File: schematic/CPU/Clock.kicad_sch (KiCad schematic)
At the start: 26 parts, among them SW1 SW_SPST, SW2 SW_MEC_5G, SW3 SW_SPST, SW4 SW_SPST, SW5 SW_MEC_5G, U33 74LS14, U34 ds1813, U35 74LS273, U36 74LS08, U37 74LS32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

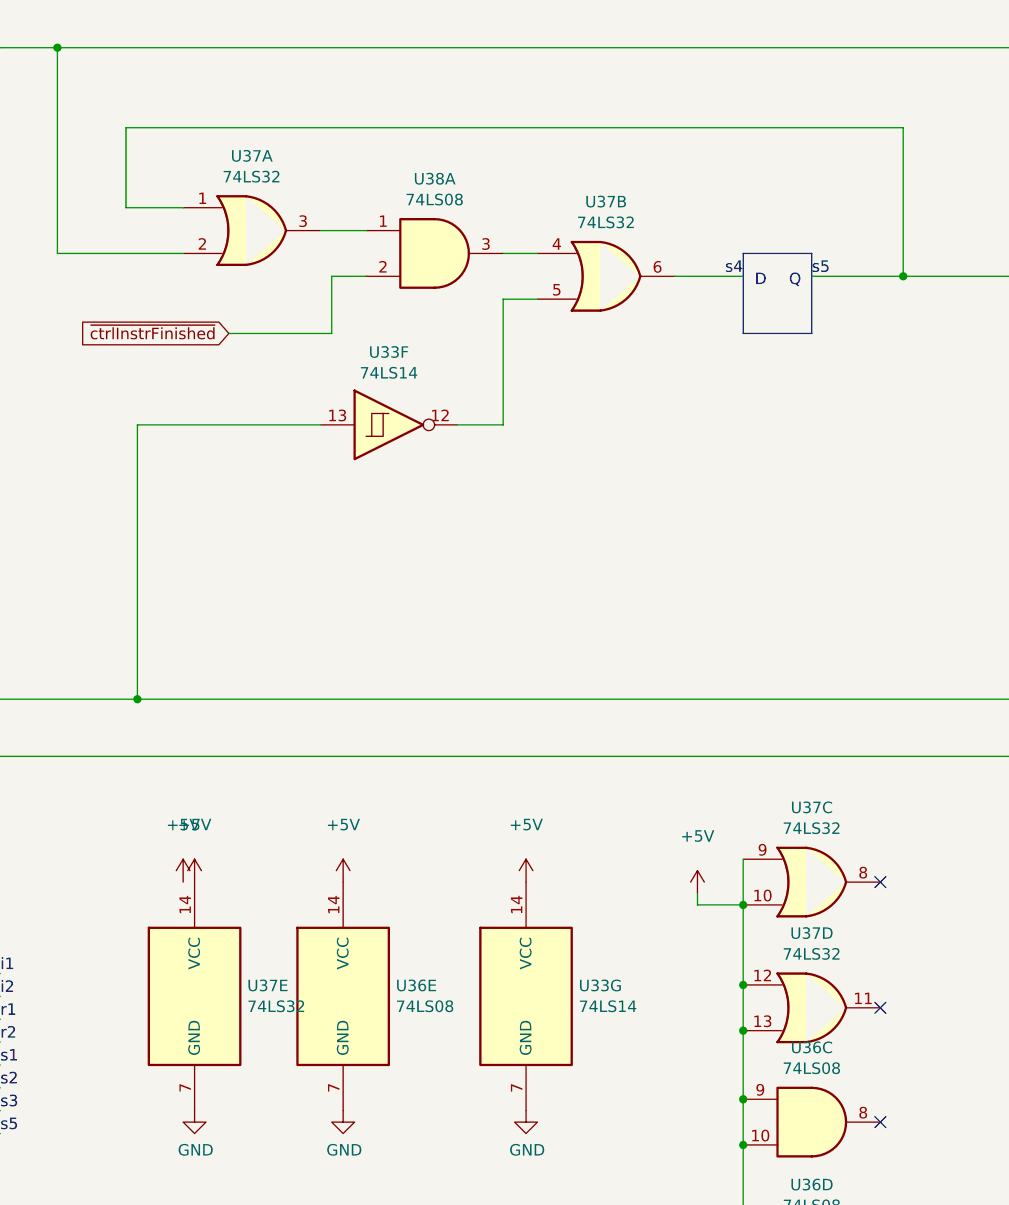
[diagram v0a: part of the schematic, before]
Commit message: ttl fpga: factorization works in sim and fpga
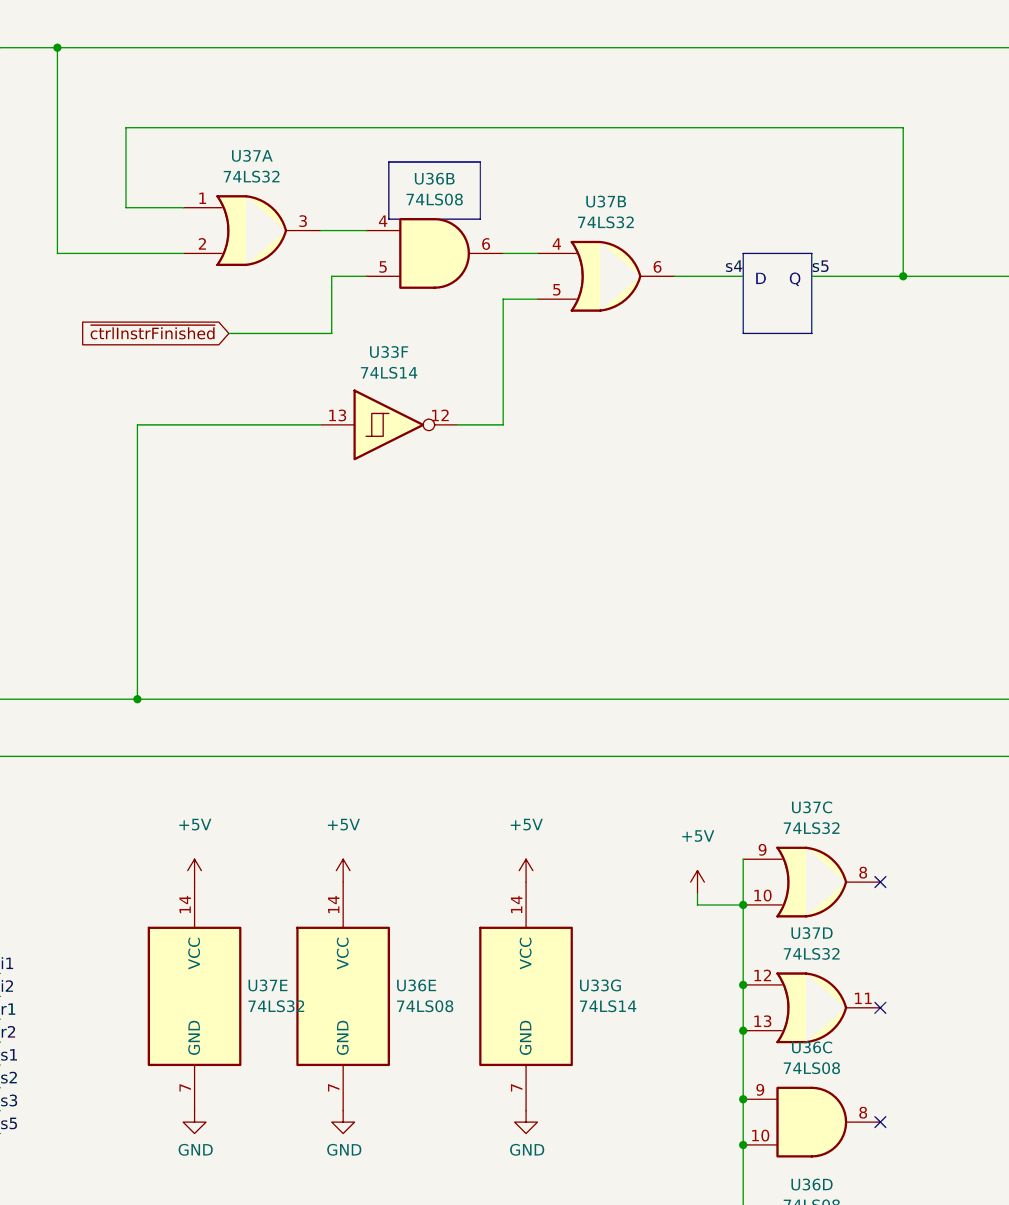
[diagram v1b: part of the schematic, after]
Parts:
- renumbered U38 to U36
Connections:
- net ~{ctrlInstrFinished}: now also U36.5; no longer U36.2
- net at U37.3: now also U36.4; no longer U36.1
- net at U37.4: now also U36.6; no longer U36.3
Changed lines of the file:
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@@
     (stroke (width 0) (type default) (color 0 0 0 0))
+  )
+  (polyline (pts (xy 201.93 50.8) (xy 201.93 44.45))
+    (stroke (width 0) (type default) (color 221 133 0 1))
   )
   (wire (pts (xy 27.94 110.49) (xy 22.86 110.49))
@@
     (stroke (width 0) (type default) (color 0 0 0 0))
   )
+  (polyline (pts (xy 212.09 44.45) (xy 212.09 50.8))
+    (stroke (width 0) (type default) (color 221 133 0 1))
+  )
   (wire (pts (xy 259.08 40.64) (xy 172.72 40.64))
     (stroke (width 0) (type default) (color 0 0 0 0))
@@
     (stroke (width 0) (type default) (color 0 0 0 0))
   )
+  (polyline (pts (xy 212.09 50.8) (xy 201.93 50.8))
+    (stroke (width 0) (type default) (color 221 133 0 1))
+  )
   (polyline (pts (xy 248.92 63.5) (xy 248.92 54.61))
     (stroke (width 0) (type default) (color 0 0 0 0))
@@
   (wire (pts (xy 154.94 149.86) (xy 158.75 149.86))
     (stroke (width 0) (type default) (color 0 0 0 0))
+  )
+  (polyline (pts (xy 201.93 44.45) (xy 212.09 44.45))
+    (stroke (width 0) (type default) (color 221 133 0 1))
   )
   (polyline (pts (xy 104.14 68.58) (xy 96.52 68.58))
@@
   (global_label "clk" (shape input) (at 129.54 157.48 180) (fields_autoplaced)
     (effects (font (size 1.27 1.27)) (justify right))
-    (property "Intersheet References" "${INTERSHEET_REFS}" (id 0) (at 0 0 0)
-      (effects (font (size 1.27 1.27)) hide)
+    (property "Intersheet References" "${INTERSHEET_REFS}" (id 0) (at 124.4339 157.4006 0)
+      (effects (font (size 1.27 1.27)) (justify right) hide)
     )
   )
@@
     (pin "6")
   )
-  (symbol (lib_id "74xx:74LS08") (at 207.01 54.61 0) (unit 1)
-    (in_bom yes) (on_board yes)
-    (property "Reference" "U38" (id 0) (at 207.01 46.355 0))
+  (symbol (lib_id "74xx:74LS08") (at 207.01 54.61 0) (unit 2)
+    (in_bom yes) (on_board yes)
+    (property "Reference" "U36" (id 0) (at 207.01 46.355 0))
     (property "Value" "74LS08" (id 1) (at 207.01 48.6664 0))
     (property "Footprint" "" (id 2) (at 207.01 54.61 0)
@@
       (effects (font (size 1.27 1.27)) hide)
     )
-    (pin "1")
-    (pin "2")
-    (pin "3")
+    (pin "4")
+    (pin "5")
+    (pin "6")
   )
   (symbol (lib_id "74xx:74LS14") (at 201.93 73.66 0) (unit 6)
@@
       (effects (font (size 1.27 1.27)) hide)
     )
-    (pin "1")
-  )
-  (symbol (lib_id "power:+5V") (at 179.07 124.46 0) (unit 1)
-    (in_bom yes) (on_board yes)
-    (property "Reference" "#PWR0121" (id 0) (at 179.07 128.27 0)
-      (effects (font (size 1.27 1.27)) hide)
-    )
-    (property "Value" "+5V" (id 1) (at 179.07 118.11 0))
-    (property "Footprint" "" (id 2) (at 179.07 124.46 0)
-      (effects (font (size 1.27 1.27)) hide)
-    )
-    (property "Datasheet" "" (id 3) (at 179.07 124.46 0)
-      (effects (font (size 1.27 1.27)) hide)
-    )
